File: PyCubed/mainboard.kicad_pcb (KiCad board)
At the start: 4 copper layers, 90.2 x 95.9 mm, 264 parts, among them IC1 MAX1771ESA+, IC2 PCF8523T_1,118, J1 503182-1852, J10 1985807, J11 73412-0114, J12 73412-0114, J13 USB_C_Receptacle_USB2.0, J14 Conn_01x06, J16 1985807, J17 1985807, J18 1985807, J19 F3311A7H121014E200, J2 Conn_01x05, J20 F3311A7H121014E200, J21 F3311A7H121014E200, J22 F3311A7H121014E200, J3 1985807, J4 1985807, J7 73412-0114, J8 Conn_01x09, J9 1985807, Q1 IRLML2803, Q10 IRLML2803, Q11 MMDT2907, Q12 BSS138DWQ-7, Q13 BSS138DWQ-7, Q14 MBT2222ADW1T1, Q15 MBT2222ADW1T1, Q16 MBT2222ADW1T1, Q17 BSS138DWQ-7, Q18 BSS138DWQ-7, Q19 BSS138DWQ-7, Q2 MBT2222ADW1T1, Q20 MBT2222ADW1T1, Q21 IRLML2803, Q22 NDS8434, Q23 MBT2222ADW1T1, Q24 SQS141ELNW-T1_GE3, Q25 2SC4713KT146R, Q26 2SC4713KT146R, Q27 NDS8434, Q28 MBT2222ADW1T1, Q29 BSS138DWQ-7, Q3 MBT2222ADW1T1, Q30 MBT2222ADW1T1, Q4 BSS138DWQ-7, Q5 MBT2222ADW1T1, Q6 BSS138DWQ-7, Q7 MBT2222ADW1T1, Q8 MBT2222ADW1T1, Q9 IRFR320TRPBF-BE3, SW1 KMR231NG LFS, U1 MAX706RESA, U10 XTB-40, U12 XTB-40, U13 EP2W+, U14 S1216V8, U17 BQ25883RGER, U18 ADM1176-1ARMZ-R7, U2 ATSAMD51J19A-AU, U21 TPS7A4501DCQT, U23 RFM98PW, U3 BMX160, U4 ADM1176-1ARMZ-R7, U5 TPS54226PWPRPWP14_2P31X2P46-L, U6 LTC4121, U7 KF50BD-TR, U8 MR25H40MDF, Y1 32.768kHz

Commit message: PyCubed Schematic Finalized
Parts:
- added C57: 10nF, Capacitor_SMD:C_0603_1608Metric, F.Cu at (263.5, 61.8)
- added C58: 10nF, Capacitor_SMD:C_0603_1608Metric, F.Cu at (263.5, 64.3)
- added C59: CPH3225A, SamacSys_Parts:CPH3225A, F.Cu at (264.6, 75.7)
- added C60: 1uF, Capacitor_SMD:C_0603_1608Metric, F.Cu at (263.5, 66.8)
- added C61: 0.1uF, Capacitor_SMD:C_0603_1608Metric, F.Cu at (205.5, 143.7)
- added D4: MBR0540T1G, SamacSys_Parts:SOD3716X135N, F.Cu at (261.9, 102.2)
- added D6: MBR0540T1G, SamacSys_Parts:SOD3716X135N, F.Cu at (261.9, 106.6)
- added IC3: UA741IDT, mainboard:SOIC127P600X175-8N, F.Cu at (211.7, 145.8)
- added J15: F3311A7H121014E200, SamacSys_Parts:F3311A7H121014E200, B.Cu at (143.4, 56.3)
- added J23: F3311A7H121014E200, SamacSys_Parts:F3311A7H121014E200, B.Cu at (143.4, 144.5)
- added J5: F3311A7H121014E200, SamacSys_Parts:F3311A7H121014E200, B.Cu at (102.7, 100.3)
- added J6: F3311A7H121014E200, SamacSys_Parts:F3311A7H121014E200, B.Cu at (182.1, 100.3)
- added JP1: SolderJumper_2_Open, Jumper:SolderJumper-2_P1.3mm_Open_Pad1.0x1.5mm, B.Cu at (141.3, 121.5)
- added JP2: SolderJumper_2_Open, Jumper:SolderJumper-2_P1.3mm_Open_Pad1.0x1.5mm, B.Cu at (141.3, 125.0)
- added JP3: SolderJumper_2_Open, Jumper:SolderJumper-2_P1.3mm_Open_Pad1.0x1.5mm, B.Cu at (141.3, 128.6)
- added JP4: SolderJumper_2_Open, Jumper:SolderJumper-2_P1.3mm_Open_Pad1.0x1.5mm, B.Cu at (141.3, 132.1)
- added JP5: SolderJumper_2_Open, Jumper:SolderJumper-2_P1.3mm_Open_Pad1.0x1.5mm, B.Cu at (141.3, 135.7)
- added JP7: SolderJumper_2_Open, Jumper:SolderJumper-2_P1.3mm_Open_Pad1.0x1.5mm, F.Cu at (204.8, 130.8)
- added JP8: SolderJumper_2_Open, Jumper:SolderJumper-2_P1.3mm_Open_Pad1.0x1.5mm, F.Cu at (270.7, 92.3)
- added JP9: SolderJumper_2_Open, Jumper:SolderJumper-2_P1.3mm_Open_Pad1.0x1.5mm, F.Cu at (270.7, 95.9)
- added Q31: BSS138DWQ-7, mainboard:BSS138DWQ-7, F.Cu at (275.8, 70.1)
- added Q32: MBT2222ADW1T1, Package_TO_SOT_SMD:SOT-363_SC-70-6, F.Cu at (275.7, 62.5)
- added Q33: BSS138DWQ-7, mainboard:BSS138DWQ-7, F.Cu at (275.8, 73.8)
- added Q34: MBT2222ADW1T1, Package_TO_SOT_SMD:SOT-363_SC-70-6, F.Cu at (275.7, 66.3)
- added R107: 100K, Resistor_SMD:R_0603_1608Metric, F.Cu at (263.5, 69.3)
- added R127: 680, Resistor_SMD:R_0603_1608Metric, F.Cu at (263.5, 71.8)
- added R128: 10K, Resistor_SMD:R_0603_1608Metric, F.Cu at (267.5, 61.8)
- added R129: 10K, Resistor_SMD:R_0603_1608Metric, F.Cu at (267.5, 64.3)
- added R130: 200K, Resistor_SMD:R_0603_1608Metric, F.Cu at (267.5, 66.8)
- added R131: 100K, Resistor_SMD:R_0603_1608Metric, F.Cu at (267.5, 69.3)
- added R132: 680, Resistor_SMD:R_0603_1608Metric, F.Cu at (267.5, 71.8)
- added R133: 10K, Resistor_SMD:R_0603_1608Metric, F.Cu at (271.5, 61.8)
- added R134: 10K, Resistor_SMD:R_0603_1608Metric, F.Cu at (271.5, 64.3)
- added R135: 200K, Resistor_SMD:R_0603_1608Metric, F.Cu at (271.5, 66.8)
- added R136: ERA-8VEB1500V, SamacSys_Parts:ERA8KEB1004V, F.Cu at (262.7, 92.9)
- added R137: ERA-8VEB1500V, SamacSys_Parts:ERA8KEB1004V, F.Cu at (262.7, 97.6)
- added R138: 100K, Resistor_SMD:R_0603_1608Metric, F.Cu at (205.5, 146.2)
- added R139: 10K, Resistor_SMD:R_0603_1608Metric, F.Cu at (205.5, 148.8)
- added R140: 10K, Resistor_SMD:R_0603_1608Metric, F.Cu at (205.5, 151.3)
- added R141: 10K, Resistor_SMD:R_0603_1608Metric, F.Cu at (205.5, 153.8)
- added R142: 100K, Resistor_SMD:R_0603_1608Metric, F.Cu at (205.5, 156.3)
- added R143: 10K, Resistor_SMD:R_0603_1608Metric, F.Cu at (205.5, 158.8)
- added R144: ERA-8PEB6803V, SamacSys_Parts:ERA8P, F.Cu at (211.4, 151.4)
- added R145: 10K, Resistor_SMD:R_0603_1608Metric, F.Cu at (205.5, 161.3)
- moved J9 89.4 mm to (170.0, 63.3)
- moved Q22 2.74 mm to (136.3, 132.1)
- moved R24 2.74 mm to (135.7, 125.9)
- moved J19 1.17 mm to (102.9, 100.3)
- moved J22 1.01 mm to (143.3, 144.5)
- moved D2 0.84 mm to (181.3, 106.5)
- moved J21 0.34 mm to (118.7, 57.2)
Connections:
- J19 pad 10: GND -> Net-(JP9-B)
- J19 pad 11: unconnected-(J19-Pad11) -> Net-(JP8-B)
- J19 pad 12: unconnected-(J19-Pad12) -> PB07
- J19 pad 13: unconnected-(J19-Pad13) -> PB09
- J19 pad 14: unconnected-(J19-Pad14) -> PB14
- J19 pad MP1: unconnected-(J19-PadMP1) -> GND
- J19 pad MP2: unconnected-(J19-PadMP2) -> GND
- U14 pad 18: unconnected-(U14-SDA/NC-Pad18) -> Net-(JP1-B)
- U14 pad 19: unconnected-(U14-SCL/NC-Pad19) -> Net-(JP2-B)
- U14 pad 20: RX -> Net-(JP3-B)
- U14 pad 21: TX -> Net-(JP4-B)
- U14 pad 22: GPS_PWR_IN -> Net-(JP5-B)
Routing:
- net VBATT: track 175.7 -> 298.4 mm, vias 10 -> 32
- net GND: track 104.4 -> 225.5 mm, vias 169 -> 183
- net 3.3V: track 84.3 -> 140.3 mm
- net RX: track 29.4 -> 0.00 mm, vias 2 -> 0
- net TX: track 29.4 -> 0.00 mm, vias 2 -> 0
- net SCL2: track 0.00 -> 26.4 mm, vias 0 -> 1
- net Net-(JP5-B): track 0.00 -> 19.1 mm
- net Net-(JP3-B): track 0.00 -> 17.7 mm
- net Net-(JP4-B): track 0.00 -> 16.3 mm
- net Net-(JP2-B): track 0.00 -> 15.3 mm
- net Net-(JP1-B): track 0.00 -> 13.0 mm
- net SDA2: track 0.00 -> 6.92 mm, vias 0 -> 1
- net VBUS_IN: track 26.1 -> 29.7 mm
- net Net-(U14-RSTN): track 18.2 -> 21.0 mm
- net Net-(Q1-D): track 4.16 -> 6.89 mm
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- added copper zone on B.Cu, net VSOLAR
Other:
- board text added: "X+"
- board text added: "X-"
- board text added: "Y+"
- board text added: "Y-"
- board text removed: "ANT"

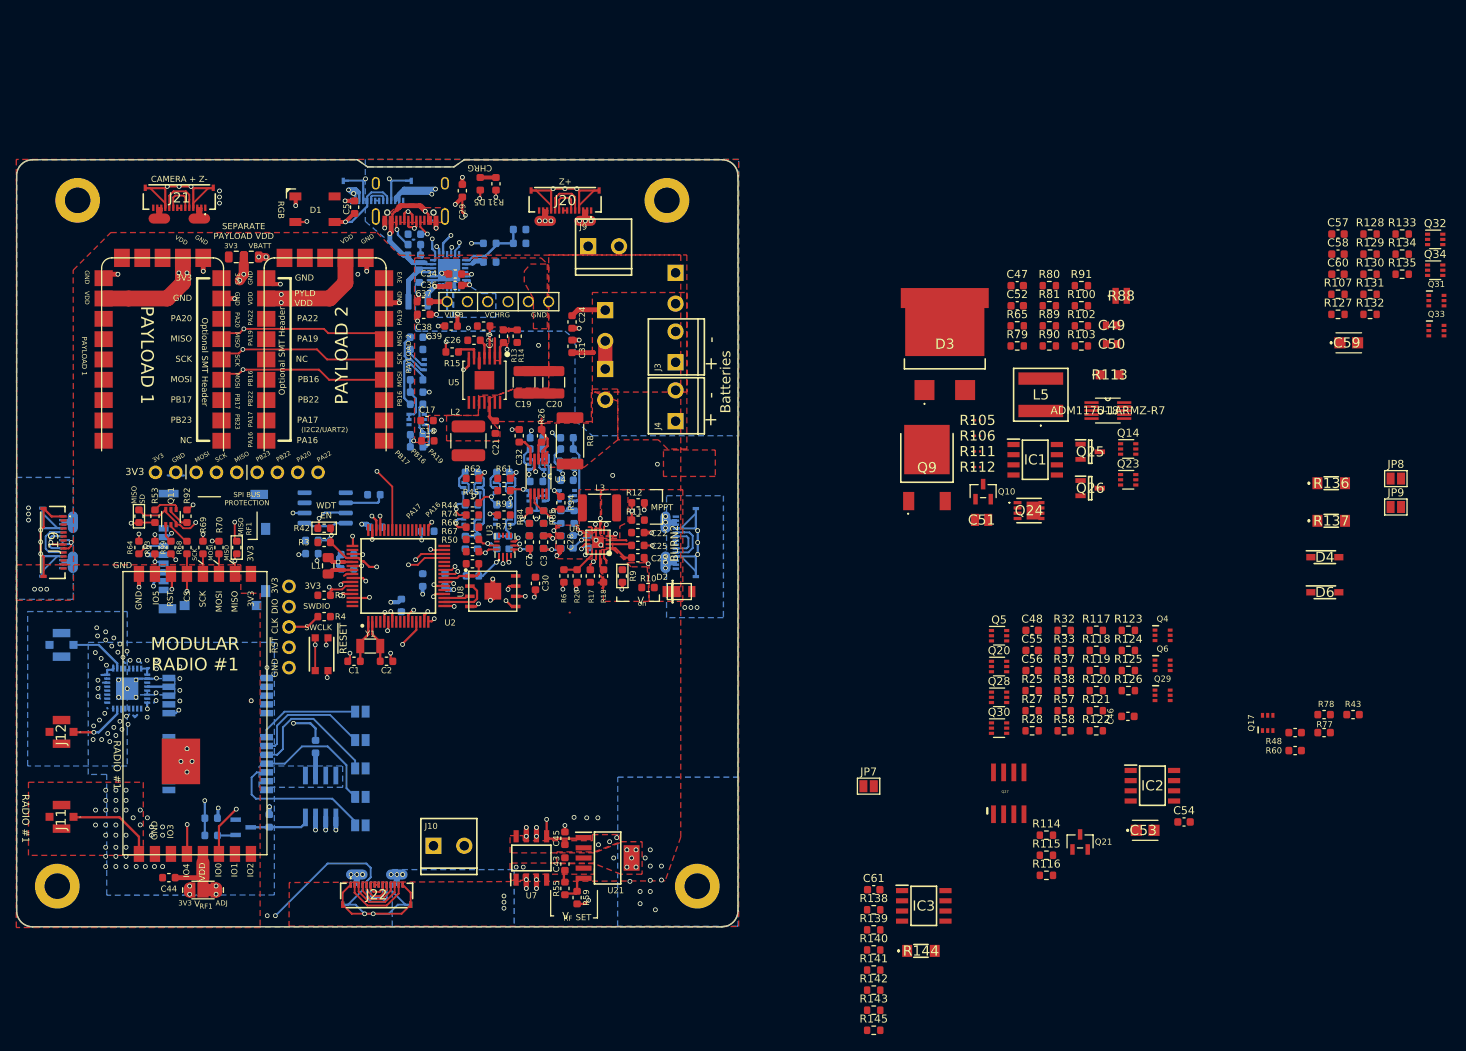
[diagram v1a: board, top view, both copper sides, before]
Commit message: PyCubed Interface Connectors Placed
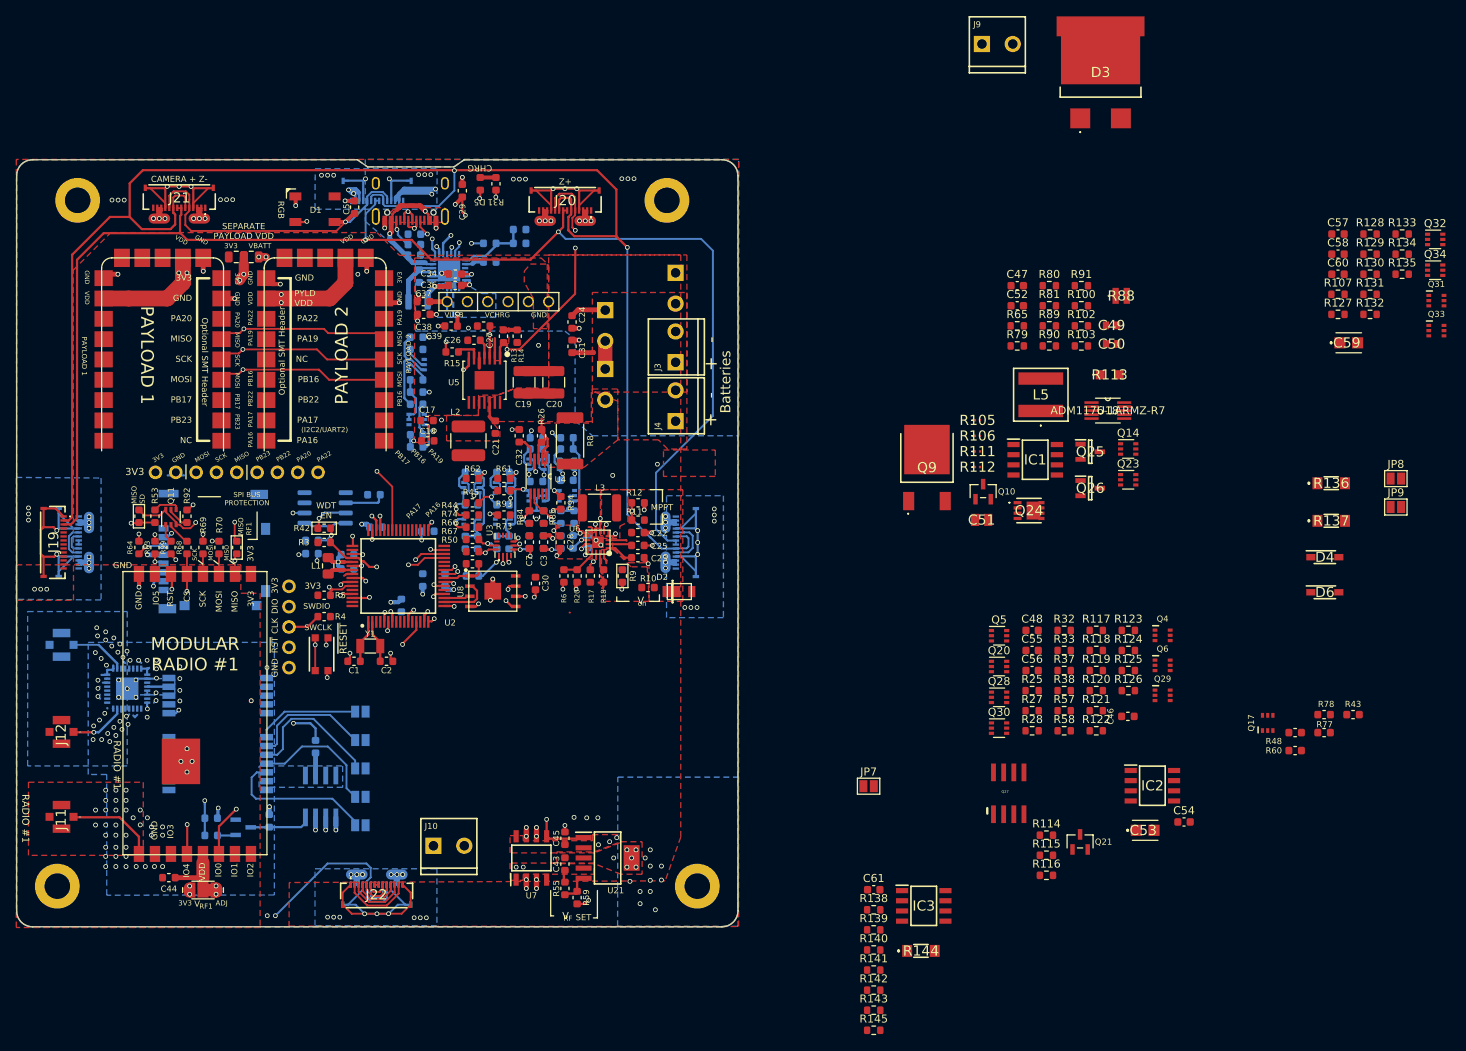
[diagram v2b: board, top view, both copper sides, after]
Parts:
- moved J9 55.3 mm to (219.2, 38.0)
- moved D3 39.2 mm to (233.8, 41.5)
- moved J5 2.04 mm to (104.8, 100.3)
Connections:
- J19 pad 2: JETSON_RX -> SCL2
- J19 pad 3: JETSON_XCK -> SDA2
- J19 pad 4: JETSON_TX -> DAC0
- J19 pad 7: DAC0 -> JETSON_RX
- J19 pad 8: SCL2 -> JETSON_XCK
- J19 pad 9: SDA2 -> JETSON_TX
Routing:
- net SCL2: track 26.4 -> 212.8 mm, vias 1 -> 2
- net SDA2: track 6.92 -> 174.3 mm, vias 1 -> 2
- net VBATT: track 298.4 -> 362.9 mm, vias 32 -> 44
- net 3.3V: track 140.3 -> 183.8 mm, vias 25 -> 27
- net VSOLAR: track 0.00 -> 30.2 mm, vias 15 -> 36
- net GNDREF: track 13.6 -> 17.5 mm
- net GND: track 225.5 -> 229.1 mm
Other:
- board text removed: "BURN2"
